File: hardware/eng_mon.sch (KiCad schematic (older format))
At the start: 1 part

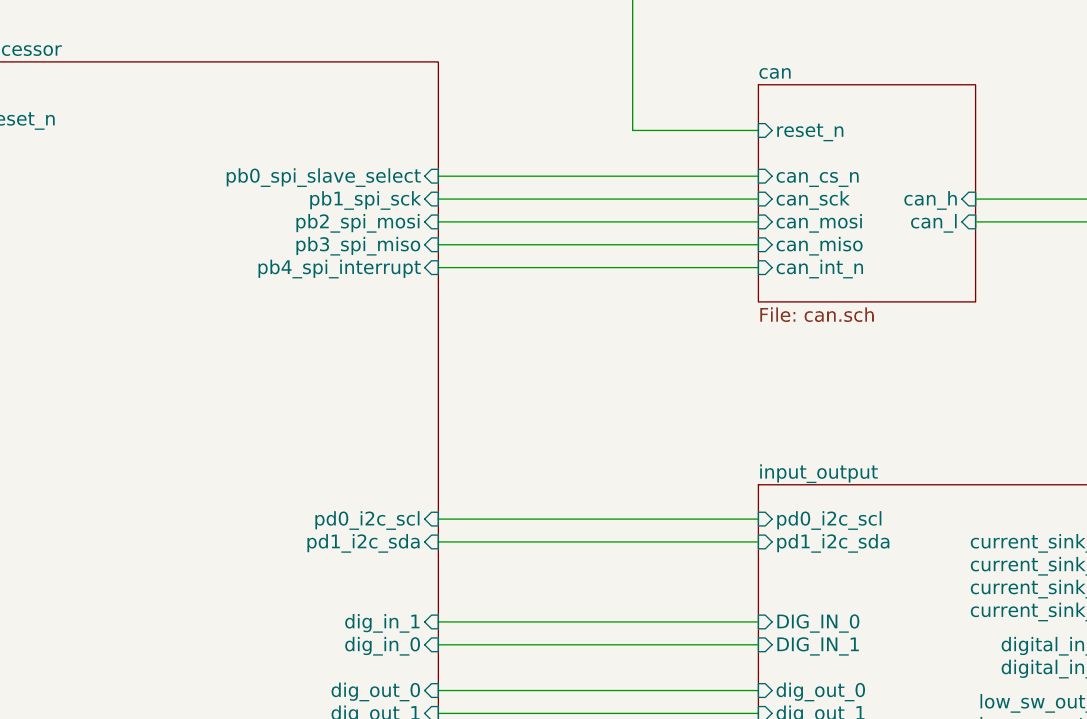
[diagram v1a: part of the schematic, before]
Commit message: changed heirarchy labels, changed diode and inductor to standard library symbols
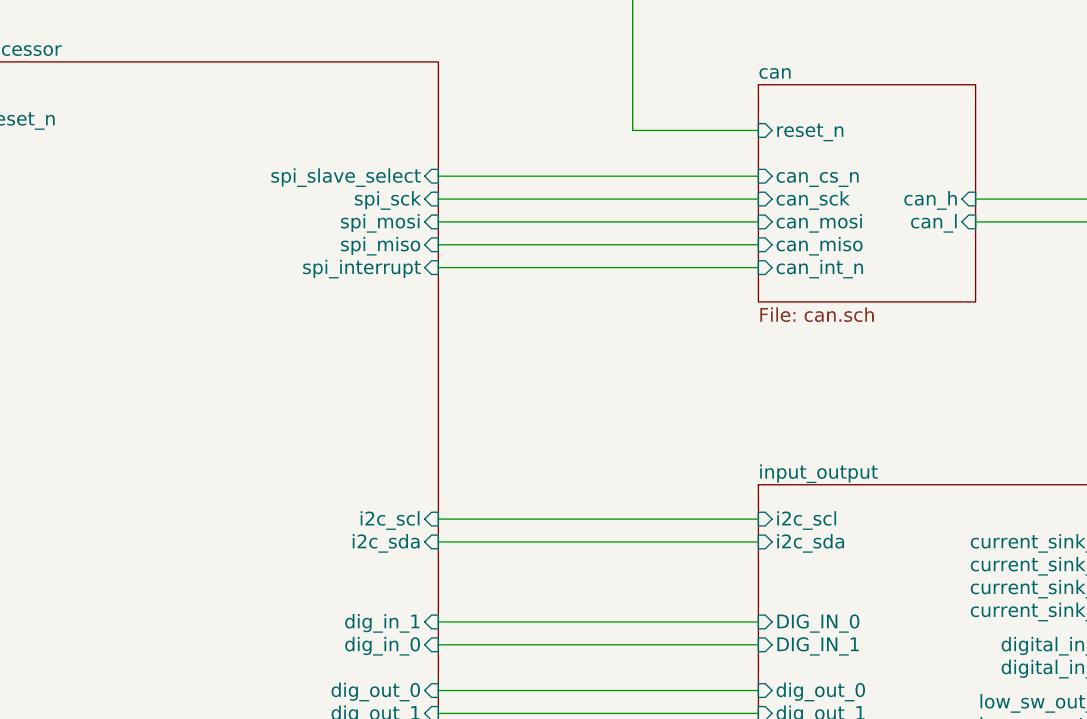
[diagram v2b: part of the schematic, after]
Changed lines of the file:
@@
-EESchema Schematic File Version 2  date Thu 31 Oct 2013 01:30:22 PM EDT
+EESchema Schematic File Version 2  date Mon 04 Nov 2013 07:38:03 AM EST
 LIBS:power
 LIBS:device
@@
 Sheet 1 5
 Title ""
-Date "31 oct 2013"
+Date "4 nov 2013"
 Rev ""
 Comp ""
@@
 F0 "input_output" 60
 F1 "in_out.sch" 60
-F2 "pd1_i2c_sda" I L 7100 4950 60
-F3 "pd0_i2c_scl" I L 7100 4850 60
+F2 "i2c_sda" I L 7100 4950 60
+F3 "i2c_scl" I L 7100 4850 60
 F4 "input_voltage" I L 7100 5950 60
 F5 "current_sink_3" I R 8700 5250 60
@@
 F0 "processor" 60
 F1 "processor.sch" 60
-F2 "pd1_i2c_sda" I R 5700 4950 60
-F3 "pd0_i2c_scl" I R 5700 4850 60
-F4 "pb4_spi_interrupt" I R 5700 3750 60
-F5 "pb3_spi_miso" I R 5700 3650 60
-F6 "pb2_spi_mosi" I R 5700 3550 60
-F7 "pb1_spi_sck" I R 5700 3450 60
-F8 "pb0_spi_slave_select" I R 5700 3350 60
+F2 "i2c_sda" I R 5700 4950 60
+F3 "i2c_scl" I R 5700 4850 60
+F4 "spi_interrupt" I R 5700 3750 60
+F5 "spi_miso" I R 5700 3650 60
+F6 "spi_mosi" I R 5700 3550 60
+F7 "spi_sck" I R 5700 3450 60
+F8 "spi_slave_select" I R 5700 3350 60
 F9 "reset_n" I L 3650 3100 60
 F10 "dig_out_0" I R 5700 5600 60

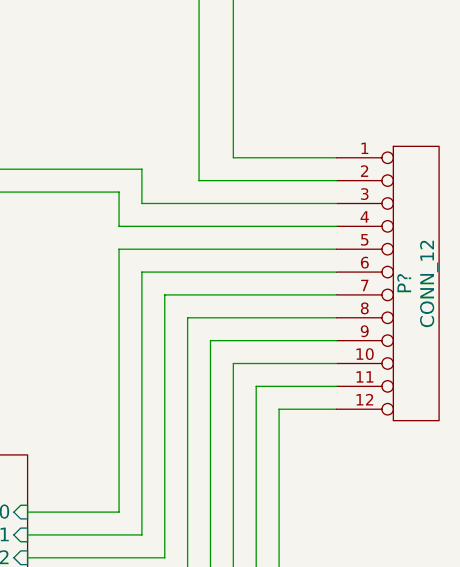
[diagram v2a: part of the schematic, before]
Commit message: cleaned up most of the error check problems
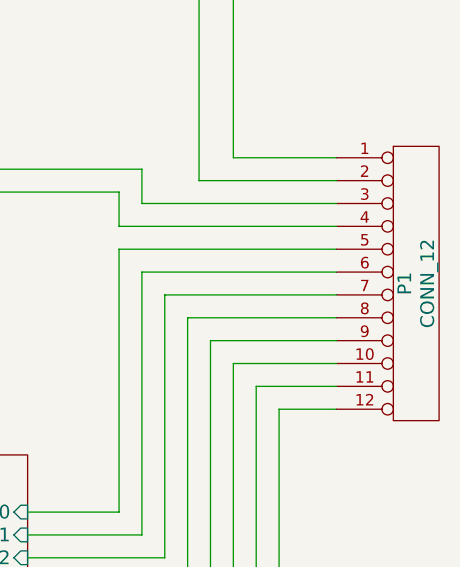
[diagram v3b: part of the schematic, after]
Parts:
- gave numbers to parts that had none: 1
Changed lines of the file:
@@
-EESchema Schematic File Version 2  date Mon 04 Nov 2013 07:38:03 AM EST
+EESchema Schematic File Version 2  date Mon 04 Nov 2013 11:57:20 AM EST
 LIBS:power
 LIBS:device
@@
 	950  1900 1350 1900
 $Comp
-L CONN_12 P?
+L CONN_12 P1
 U 1 1 526DB75C
 P 10400 3950
-F 0 "P?" V 10350 3950 60  0000 C CNN
+F 0 "P1" V 10350 3950 60  0000 C CNN
 F 1 "CONN_12" V 10450 3950 60  0000 C CNN
 	1    10400 3950

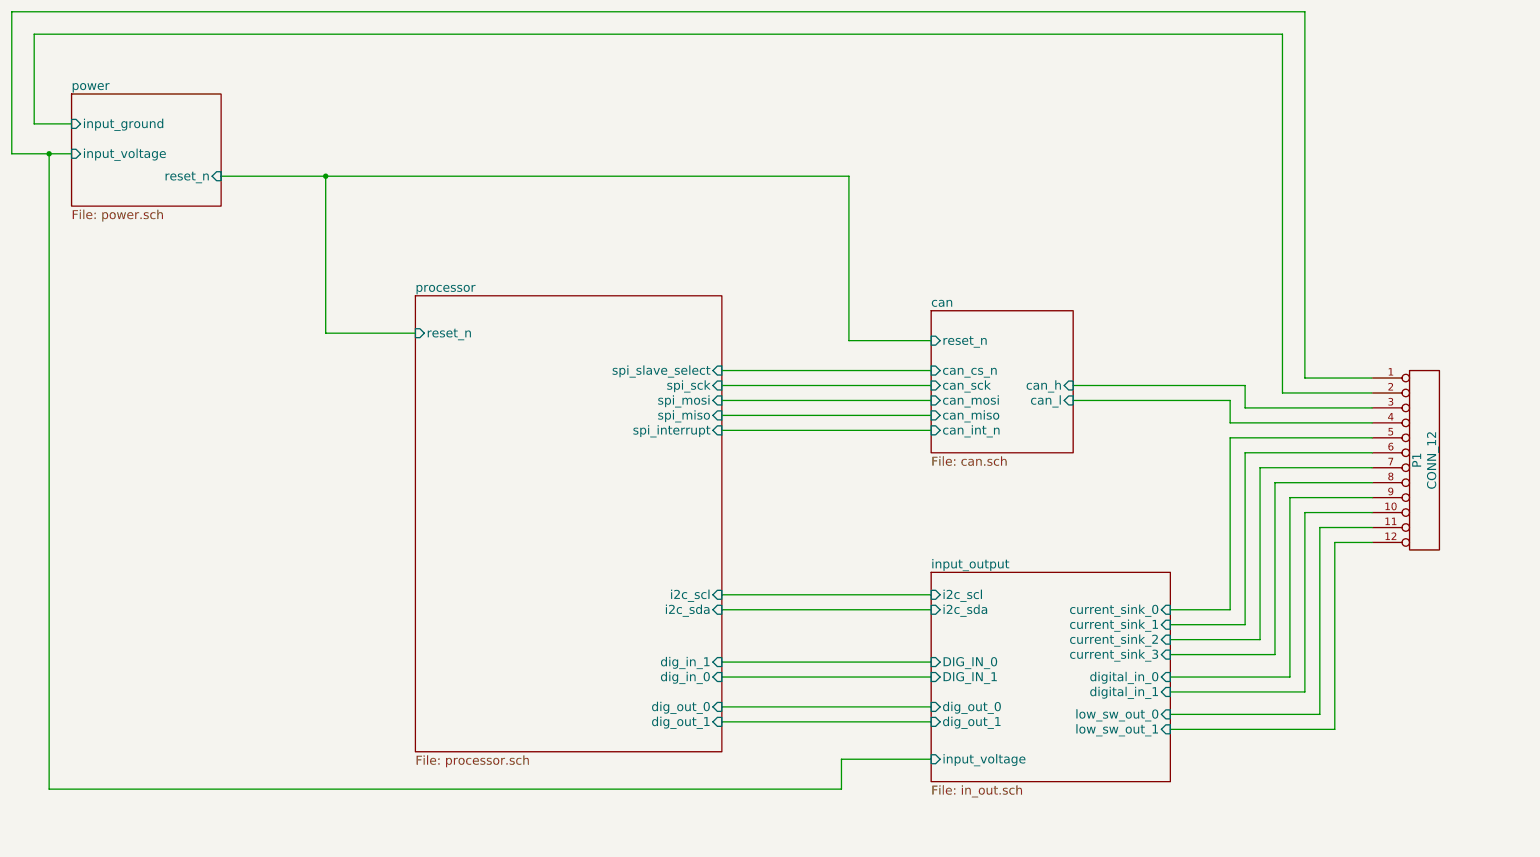
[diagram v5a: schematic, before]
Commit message: added RCT and accellerometer, added new sheet
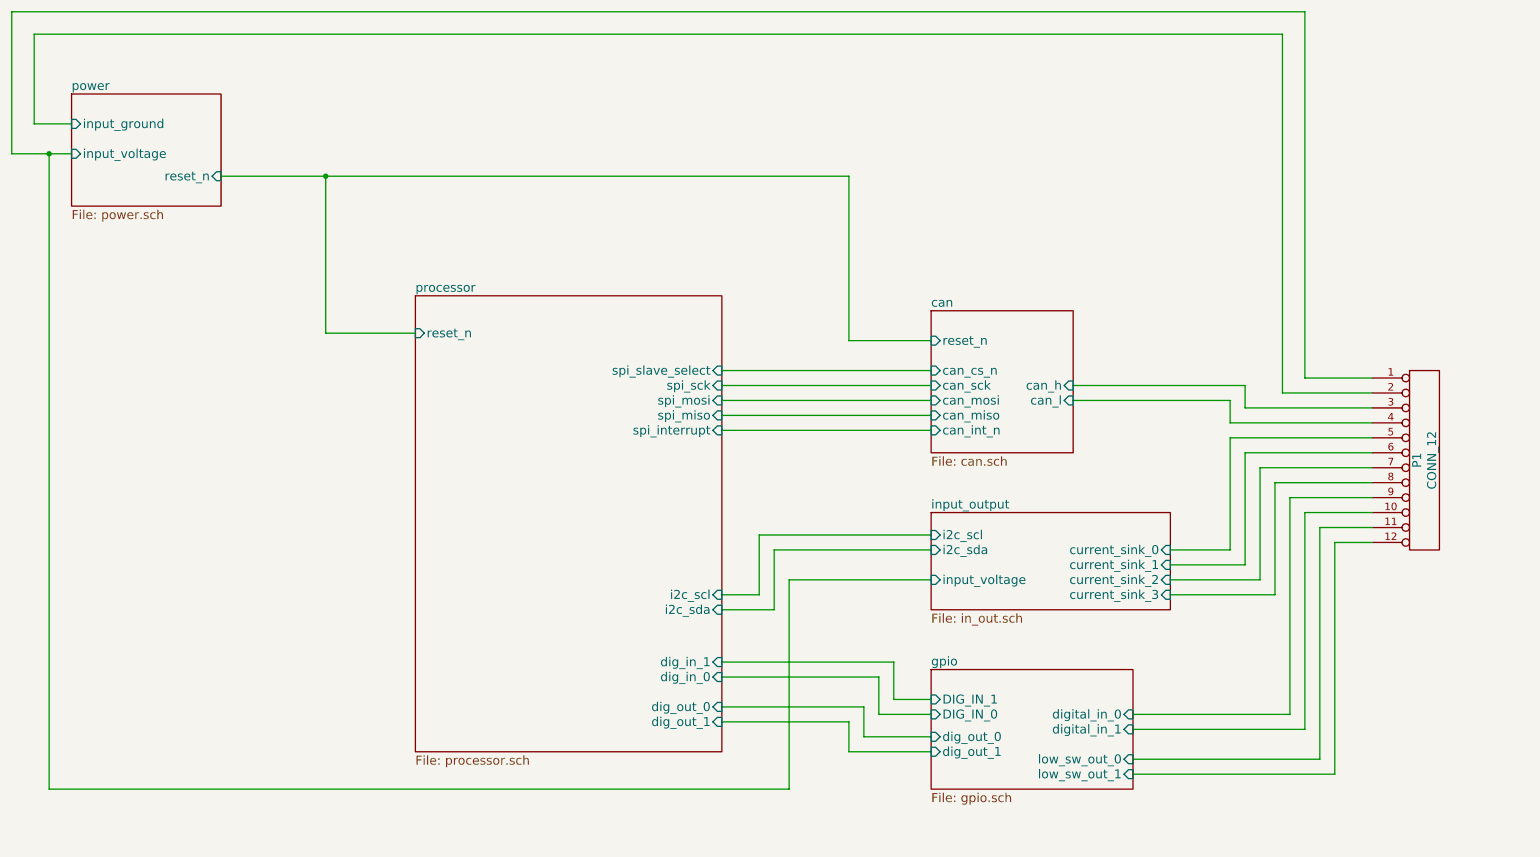
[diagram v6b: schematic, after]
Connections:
- net input_output/digital_in_0 renamed gpio/digital_in_0
- net input_output/digital_in_1 renamed gpio/digital_in_1
- net input_output/low_sw_out_0 renamed gpio/low_sw_out_0
- net input_output/low_sw_out_1 renamed gpio/low_sw_out_1
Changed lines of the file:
@@
-EESchema Schematic File Version 2  date Thu 07 Nov 2013 07:55:20 AM EST
+EESchema Schematic File Version 2  date Tue 12 Nov 2013 10:09:33 PM EST
 LIBS:power
 LIBS:device
@@
 $Descr A4 11700 8267
 encoding utf-8
-Sheet 1 5
+Sheet 1 6
 Title ""
-Date "7 nov 2013"
+Date "13 nov 2013"
 Rev ""
 Comp ""
@@
 Comment4 ""
 $EndDescr
+Wire Wire Line
+	7100 5900 6550 5900
+Wire Wire Line
+	6550 5900 6550 5700
+Wire Wire Line
+	6550 5700 5700 5700
+Wire Wire Line
+	7100 5650 6750 5650
+Wire Wire Line
+	6750 5650 6750 5400
+Wire Wire Line
+	6750 5400 5700 5400
+Wire Wire Line
+	10050 4500 9800 4500
+Wire Wire Line
+	9800 4500 9800 6050
+Wire Wire Line
+	9800 6050 8450 6050
+Wire Wire Line
+	10050 4300 9600 4300
+Wire Wire Line
+	9600 4300 9600 5750
+Wire Wire Line
+	9600 5750 8450 5750
+Wire Wire Line
+	7100 4550 6050 4550
+Wire Wire Line
+	6050 4550 6050 4950
+Wire Wire Line
+	6050 4950 5700 4950
 Connection ~ 1200 1900
 Wire Wire Line
@@
 	10050 3900 9200 3900
 Wire Wire Line
-	9200 3900 9200 5050
-Wire Wire Line
-	9200 5050 8700 5050
+	9200 3900 9200 4650
+Wire Wire Line
+	9200 4650 8700 4650
 Wire Wire Line
 	10050 4100 9400 4100
 Wire Wire Line
-	9400 4100 9400 5250
-Wire Wire Line
-	9400 5250 8700 5250
-Wire Wire Line
-	10050 4300 9600 4300
-Wire Wire Line
-	9600 4300 9600 5500
-Wire Wire Line
-	9600 5500 8700 5500
-Wire Wire Line
-	8700 5750 9800 5750
-Wire Wire Line
-	9800 5750 9800 4500
-Wire Wire Line
-	9800 4500 10050 4500
-Wire Wire Line
-	5700 5700 7100 5700
-Wire Wire Line
-	5700 5400 7100 5400
+	9400 4100 9400 4850
+Wire Wire Line
+	9400 4850 8700 4850
 Wire Wire Line
 	7100 3150 6550 3150
@@
 Wire Wire Line
 	5700 3450 7100 3450
-Wire Wire Line
-	7100 4950 5700 4950
-Wire Wire Line
-	7100 4850 5700 4850
 Wire Wire Line
 	7100 3350 5700 3350
@@
 Connection ~ 3050 2050
 Wire Wire Line
-	5700 5300 7100 5300
-Wire Wire Line
-	7100 5600 5700 5600
-Wire Wire Line
-	7100 5950 6500 5950
-Wire Wire Line
-	6500 5950 6500 6150
-Wire Wire Line
-	6500 6150 1200 6150
+	7100 4750 6150 4750
+Wire Wire Line
+	6150 4750 6150 6150
+Wire Wire Line
+	6150 6150 1200 6150
 Wire Wire Line
 	1200 6150 1200 1900
 Wire Wire Line
-	8700 5650 9700 5650
-Wire Wire Line
-	9700 5650 9700 4400
+	8700 4750 9300 4750
+Wire Wire Line
+	9300 4750 9300 4000
+Wire Wire Line
+	9300 4000 10050 4000
+Wire Wire Line
+	8700 4550 9100 4550
+Wire Wire Line
+	9100 4550 9100 3800
+Wire Wire Line
+	9100 3800 10050 3800
+Wire Wire Line
+	10050 3600 9200 3600
+Wire Wire Line
+	9200 3600 9200 3450
+Wire Wire Line
+	9200 3450 8050 3450
+Wire Wire Line
+	10050 3400 9600 3400
+Wire Wire Line
+	9600 3400 9600 950
+Wire Wire Line
+	9600 950  950  950
+Wire Wire Line
+	950  950  950  1900
+Wire Wire Line
+	950  1900 1350 1900
+Wire Wire Line
+	5700 4850 5950 4850
+Wire Wire Line
+	5950 4850 5950 4450
+Wire Wire Line
+	5950 4450 7100 4450
+Wire Wire Line
+	8450 5650 9500 5650
+Wire Wire Line
+	9500 5650 9500 4200
+Wire Wire Line
+	9500 4200 10050 4200
+Wire Wire Line
+	8450 5950 9700 5950
+Wire Wire Line
+	9700 5950 9700 4400
 Wire Wire Line
 	9700 4400 10050 4400
 Wire Wire Line
-	8700 5400 9500 5400
-Wire Wire Line
-	9500 5400 9500 4200
-Wire Wire Line
-	9500 4200 10050 4200
-Wire Wire Line
-	8700 5150 9300 5150
-Wire Wire Line
-	9300 5150 9300 4000
-Wire Wire Line
-	9300 4000 10050 4000
-Wire Wire Line
-	8700 4950 9100 4950
-Wire Wire Line
-	9100 4950 9100 3800
-Wire Wire Line
-	9100 3800 10050 3800
-Wire Wire Line
-	10050 3600 9200 3600
-Wire Wire Line
-	9200 3600 9200 3450
-Wire Wire Line
-	9200 3450 8050 3450
-Wire Wire Line
-	10050 3400 9600 3400
-Wire Wire Line
-	9600 3400 9600 950
-Wire Wire Line
-	9600 950  950  950
-Wire Wire Line
-	950  950  950  1900
-Wire Wire Line
-	950  1900 1350 1900
+	5700 5300 6850 5300
+Wire Wire Line
+	6850 5300 6850 5550
+Wire Wire Line
+	6850 5550 7100 5550
+Wire Wire Line
+	5700 5600 6650 5600
+Wire Wire Line
+	6650 5600 6650 5800
+Wire Wire Line
+	6650 5800 7100 5800
+$Sheet
+S 7100 5350 1350 800
+U 5282BEA8
+F0 "gpio" 60
+F1 "gpio.sch" 60
+F2 "digital_in_1" I R 8450 5750 60
+F3 "digital_in_0" I R 8450 5650 60
+F4 "DIG_IN_1" I L 7100 5550 60
+F5 "low_sw_out_1" I R 8450 6050 60
+F6 "dig_out_1" I L 7100 5900 60
+F7 "dig_out_0" I L 7100 5800 60
+F8 "low_sw_out_0" I R 8450 5950 60
+F9 "DIG_IN_0" I L 7100 5650 60
+$EndSheet
 $Comp
 L CONN_12 P1
@@
 $EndSheet
 $Sheet
-S 7100 4700 1600 1400
+S 7100 4300 1600 650
 U 52651A40
 F0 "input_output" 60
 F1 "in_out.sch" 60
-F2 "i2c_sda" I L 7100 4950 60
-F3 "i2c_scl" I L 7100 4850 60
-F4 "input_voltage" I L 7100 5950 60
-F5 "current_sink_3" I R 8700 5250 60
-F6 "current_sink_2" I R 8700 5150 60
-F7 "current_sink_1" I R 8700 5050 60
-F8 "current_sink_0" I R 8700 4950 60
-F9 "digital_in_1" I R 8700 5500 60
-F10 "digital_in_0" I R 8700 5400 60
-F11 "DIG_IN_1" I L 7100 5400 60
-F12 "low_sw_out_1" I R 8700 5750 60
-F13 "dig_out_1" I L 7100 5700 60
-F14 "dig_out_0" I L 7100 5600 60
-F15 "low_sw_out_0" I R 8700 5650 60
-F16 "DIG_IN_0" I L 7100 5300 60
-$EndSheet
-$Sheet
+F2 "i2c_sda" I L 7100 4550 60
+F3 "i2c_scl" I L 7100 4450 60
+F4 "input_voltage" I L 7100 4750 60
+F5 "current_sink_3" I R 8700 4850 60
+F6 "current_sink_2" I R 8700 4750 60
+F7 "current_sink_1" I R 8700 4650 60
+F8 "current_sink_0" I R 8700 4550 60
+$EndSheet
+$Sheet

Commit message: fixed heirarchy connections for modified sheets
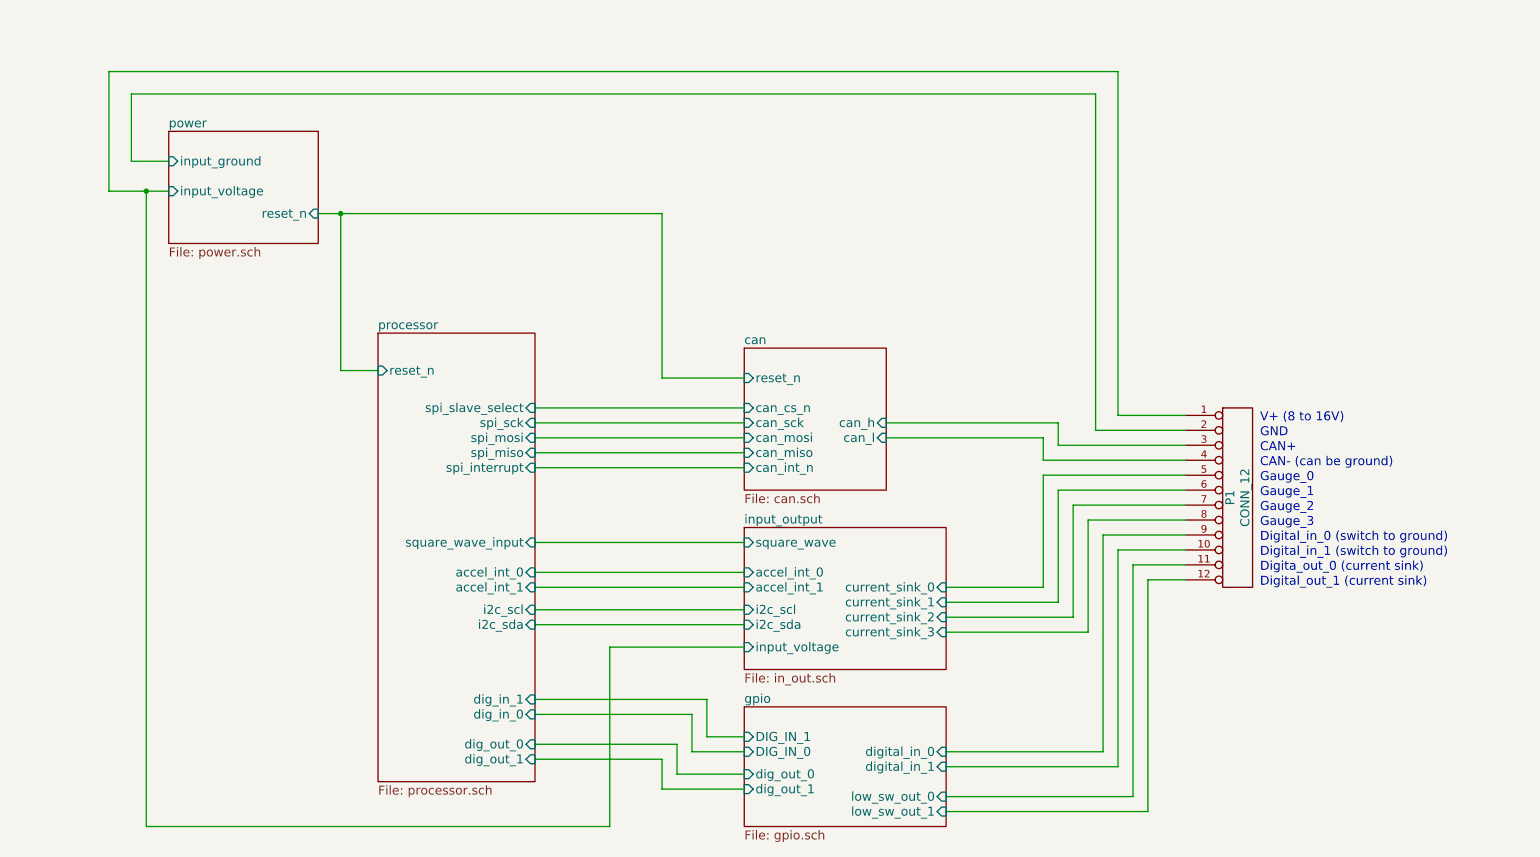
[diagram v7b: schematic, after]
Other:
- note added: "CAN+"
- note added: "CAN- (can be ground)"
- note added: "Digita_out_0 (current sink)"
- note added: "Digital_in_0 (switch to ground)"
- note added: "Digital_in_1 (switch to ground)"
- note added: "Digital_out_1 (current sink)"
- note added: "GND"
- note added: "Gauge_0"
- note added: "Gauge_1"
- note added: "Gauge_2"
- note added: "Gauge_3"
- note added: "V+ (8 to 16V)"
- moved on the sheet: P1
